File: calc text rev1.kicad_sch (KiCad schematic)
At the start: 33 parts, among them J1 Conn_ARM_SWD_TagConnect_TC203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, U1 STM32WL5MOCH6STR, U2 TLV75533PDBV

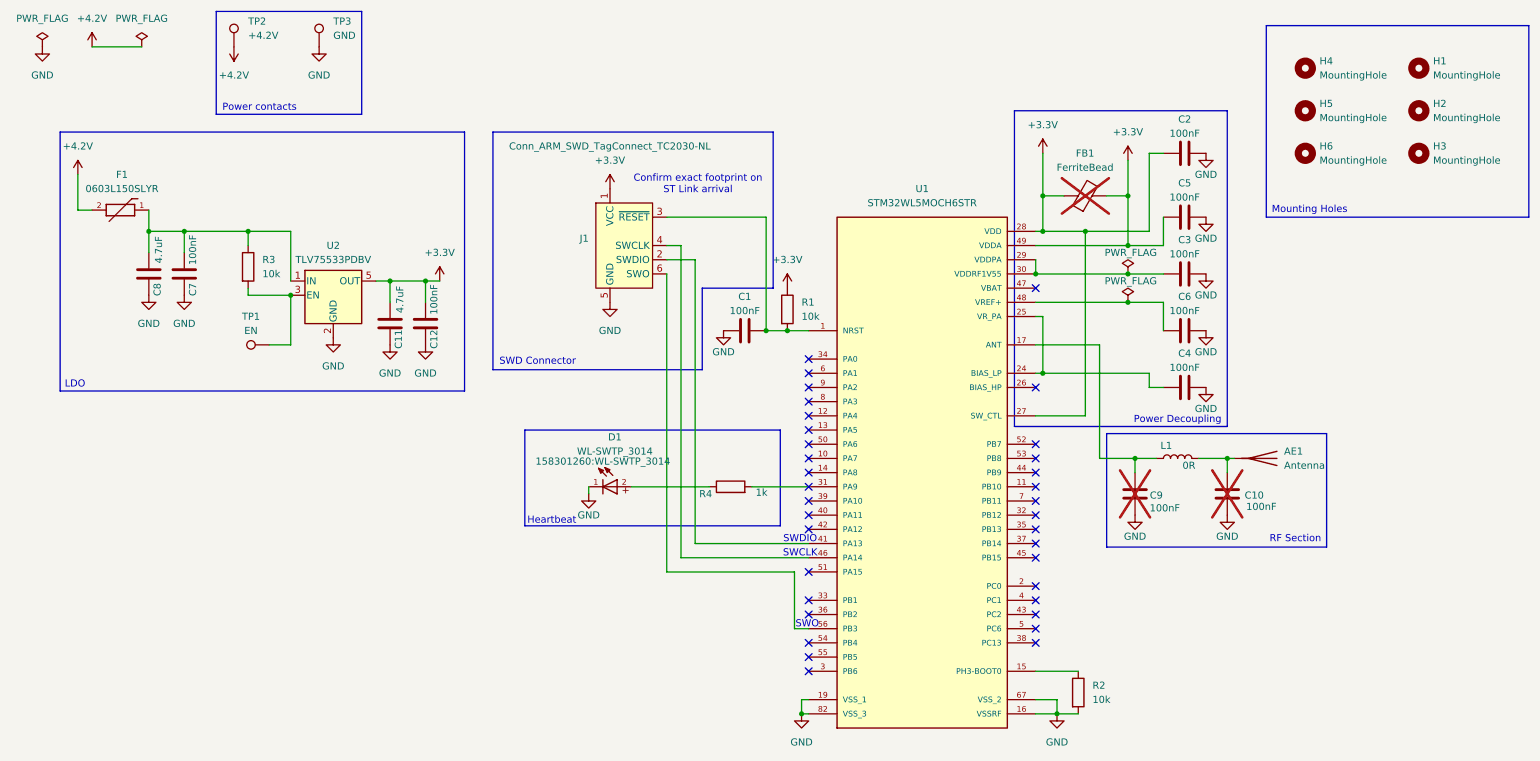
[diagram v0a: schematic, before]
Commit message: fix: move mounting holes
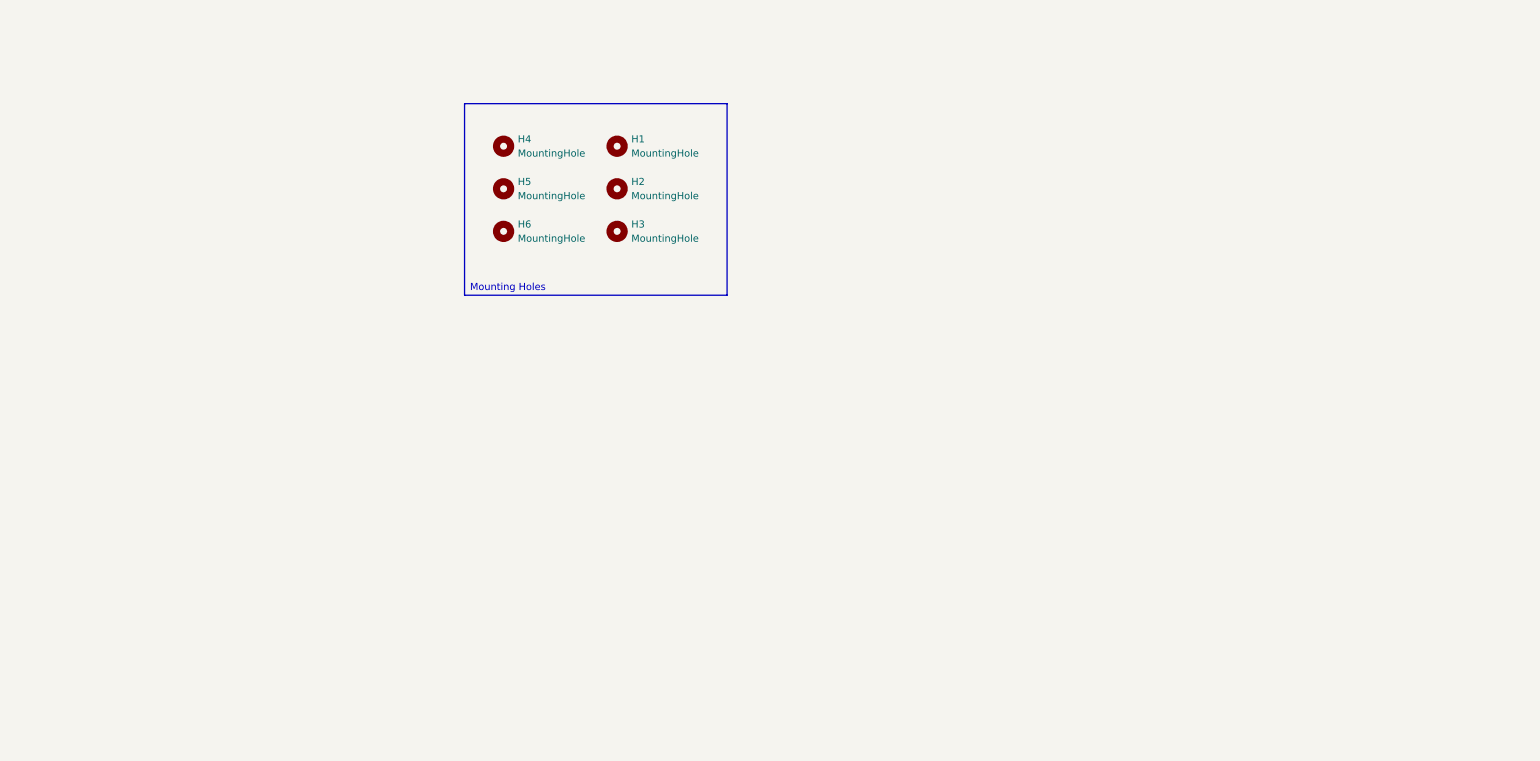
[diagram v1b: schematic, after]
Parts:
- removed AE1: Antenna, symbol Device:Antenna
- removed C1, C10, C12, C2, C3, C4, C5, C6, C7, C9: 100nF, Capacitor_SMD:C_0603_1608Metric, symbol Device:C
- removed C11, C8: 4.7uF, Capacitor_SMD:C_0603_1608Metric, symbol Device:C
- removed D1: WL-SWTP_3014, 158301260:WL-SWTP_3014, symbol 158301260:WL-SWTP_3014
- removed F1: 0603L150SLYR, Fuse:Fuse_1812_4532Metric_Pad1.30x3.40mm_HandSolder, symbol 0603L050YR:0603L150SLYR
- removed FB1: FerriteBead, symbol Device:FerriteBead
- removed J1: Conn_ARM_SWD_TagConnect_TC2030-NL, STLINKV2:STLINKV2, symbol Connector:Conn_ARM_SWD_TagConnect_TC2030-NL
- removed L1: 0R, Resistor_SMD:R_0603_1608Metric_Pad0.98x0.95mm_HandSolder, symbol Device:L
- removed R1, R2, R3: 10k, Resistor_SMD:R_0603_1608Metric_Pad0.98x0.95mm_HandSolder, symbol Device:R
- removed R4: 1k, Resistor_SMD:R_0603_1608Metric_Pad0.98x0.95mm_HandSolder, symbol Device:R
- removed TP1: EN, TestPoint:TestPoint_Pad_1.0x1.0mm, symbol Connector:TestPoint
- removed TP2: +4.2V, TestPoint:TestPoint_Pad_1.0x1.0mm, symbol Connector:TestPoint
- removed TP3: GND, TestPoint:TestPoint_Pad_1.0x1.0mm, symbol Connector:TestPoint
- removed U1: STM32WL5MOCH6STR, STM32WL5MOCH6STR:XCVR_STM32WL5MOCH6STR, symbol STM32WL5MOCH6STR:STM32WL5MOCH6STR
- removed U2: TLV75533PDBV, Package_TO_SOT_SMD:SOT-23-5, symbol Regulator_Linear:TLV75533PDBV
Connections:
- no-connect marks 35 -> 0
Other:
- note removed: "Confirm exact footprint on ST Link arrival"
- note removed: "Heartbeat"
- note removed: "LDO"
- note removed: "Power Decoupling"
- note removed: "Power contacts"
- note removed: "RF Section"
- note removed: "SWCLK"
- note removed: "SWD Connector"
- note removed: "SWDIO"
- note removed: "SWO"
- moved on the sheet: H1, H2, H3, H4, H5, H6

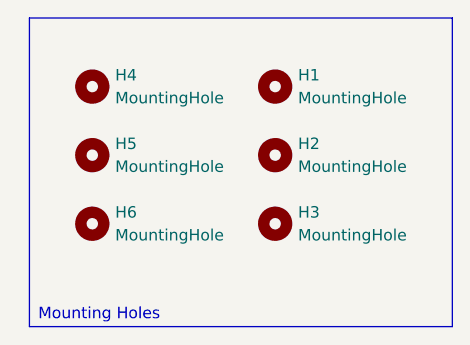
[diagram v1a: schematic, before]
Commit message: refactor: set hole size to 4.3mm
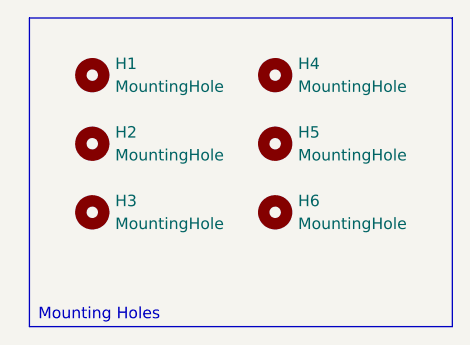
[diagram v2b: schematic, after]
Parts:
- H1, H2, H3, H4, H5, H6: footprint MountingHole:MountingHole_3.5mm_CustomFilled -> MountingHole:MountingHole_4.3mm_M4
